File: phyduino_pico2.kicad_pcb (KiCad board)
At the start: 4 copper layers, 68.6 x 53.3 mm, 139 parts, among them J1 1.0-3PWT, J2 PM2.54-1*8, J3 PM2.54-1*10, J4 PM2.54-1*6, J5 PM2.54-1*8, J6 GT-USB-7047A, J7 HC-FPC-0.5-22P-CSH20, SW1 1977067-1, SW2 MINI MSK12CO2, U1 RP2350B, U10 AP63200WU, U108 TPS2121RUXR, U11 ESP32-C6-MINI-1-H4, U110 TPS2121RUXR, U2 GD25LE128EXHIGR, U3 IS66WVR8M8FBLL-104NLI, U4 XC6190AN157R-G, U5 ADS7038QRTERQ1, U7 ZD24C64A-MAGMT, U8 AP63200WU, U9 TPUSBLC6-2P6, Y1 XC32M4-12.000-F10NNFT

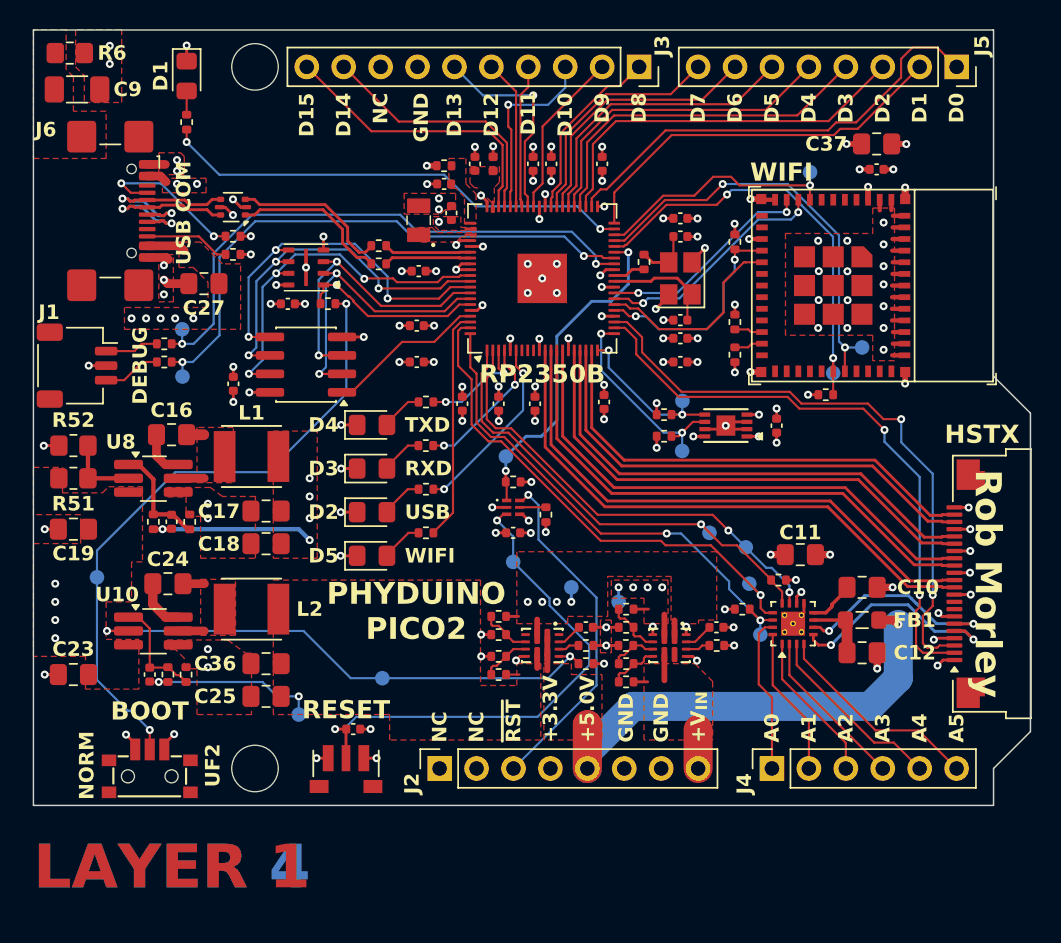
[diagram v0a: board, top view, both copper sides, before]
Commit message: Development update : Changed the power input and tree, removed led for communication status.
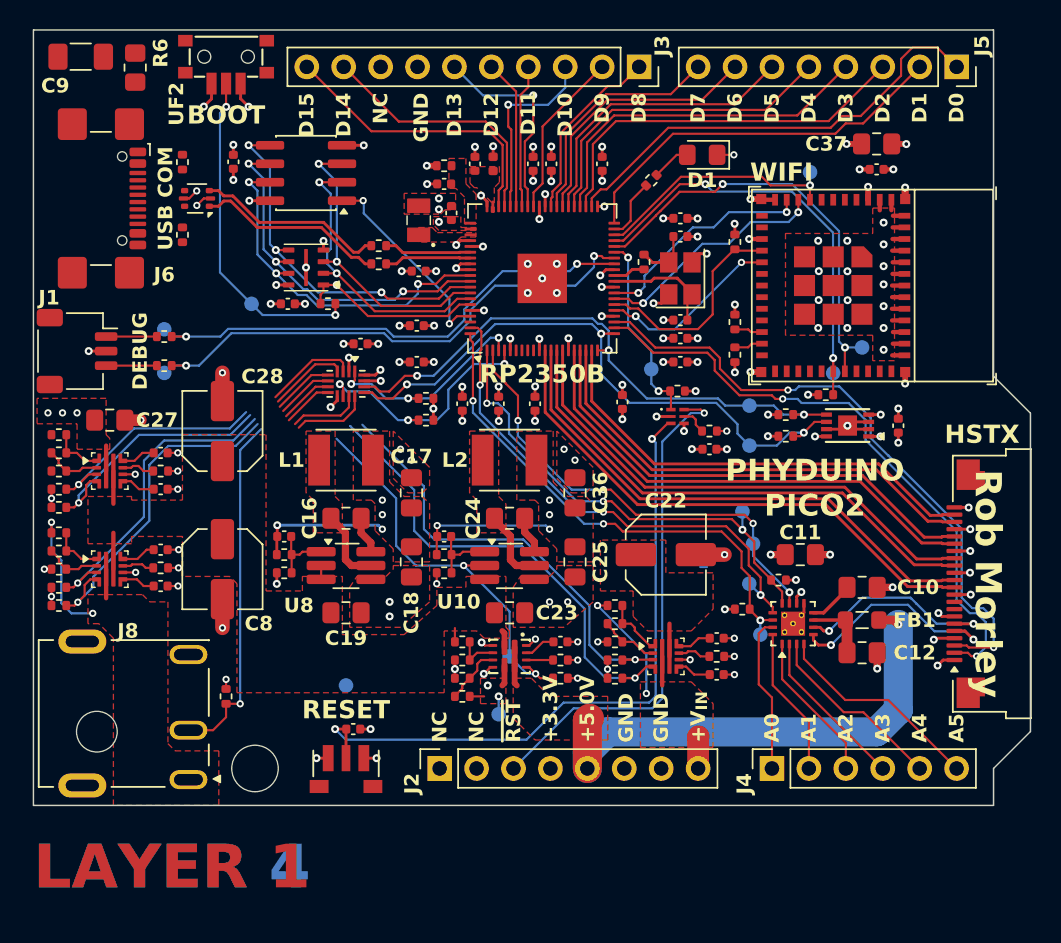
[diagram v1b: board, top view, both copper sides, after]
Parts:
- removed C134: 0.1µF, Capacitor_SMD:C_0402_1005Metric
- removed D2, D5: RED, LED_SMD:LED_0805_2012Metric_Pad1.15x1.40mm_HandSolder
- removed D3: ORANGE, LED_SMD:LED_0805_2012Metric_Pad1.15x1.40mm_HandSolder
- removed D4: GREEN, LED_SMD:LED_0805_2012Metric_Pad1.15x1.40mm_HandSolder
- removed H1: MountingHole, MountingHole [KL]:MountingHole_3.2mm_M3
- removed R140: 113kΩ, Resistor_SMD:R_0402_1005Metric
- removed R141: 432kΩ, Resistor_SMD:R_0402_1005Metric
- removed R142: 52.3kΩ, Resistor_SMD:R_0402_1005Metric
- removed R144, R145: 24.3kΩ, Resistor_SMD:R_0402_1005Metric
- removed R152: 35.7kΩ, Resistor_SMD:R_0402_1005Metric
- removed R51: 47kΩ, Resistor_SMD:R_0805_2012Metric_Pad1.20x1.40mm_HandSolder
- removed R52: 16.5kΩ, Resistor_SMD:R_0805_2012Metric_Pad1.20x1.40mm_HandSolder
- removed R53, R54, R60: 1.1kΩ, Resistor_SMD:R_0402_1005Metric
- removed TP16, TP17: TestPoint_Small, Component - Test point SMT [UL]:TestPoint_SameSky_CPG-47-TH-B
- removed U110: TPS2121RUXR, Package - QFN [UL]:VQFN-HR-12
- added C132: 0.033µF, Capacitor_SMD:C_0402_1005Metric, F.Cu at (38.5, 66.1)
- added C136: 1nF, Capacitor_SMD:C_0402_1005Metric, F.Cu at (38.5, 68.6)
- added C137: 0.033µF, Capacitor_SMD:C_0402_1005Metric, F.Cu at (76.7, 72.2)
- added C138: 1nF, Capacitor_SMD:C_0402_1005Metric, F.Cu at (76.7, 74.7)
- added C139: 0.1µF, Capacitor_SMD:C_0402_1005Metric, F.Cu at (38.5, 59.4)
- added C140: 1nF, Capacitor_SMD:C_0402_1005Metric, F.Cu at (38.5, 61.9)
- added C22: 100µF, Capacitor_SMD:C_Elec_5x5.4, F.Cu at (73.2, 66.4)
- added C28: 100µF, Capacitor_SMD:C_Elec_5x5.4, F.Cu at (42.7, 57.9)
- added C29: 0.1µF, Capacitor_SMD:C_0402_1005Metric, F.Cu at (52.2, 51.9)
- added C8: 100µF, Capacitor_SMD:C_Elec_5x5.4, F.Cu at (42.7, 67.4)
- added J8: 54-00127, Conector - Power [UL]:TENSILITY_54-00127, F.Cu at (33.1, 77.3)
- added R139: 1.1kΩ, Resistor_SMD:R_0402_1005Metric, F.Cu at (38.5, 67.3)
- added R143: 732kΩ, Resistor_SMD:R_0402_1005Metric, F.Cu at (31.5, 64.9)
- added R146: 215kΩ, Resistor_SMD:R_0402_1005Metric, F.Cu at (31.5, 66.2)
- added R147: 732kΩ, Resistor_SMD:R_0402_1005Metric, F.Cu at (69.7, 69.9)
- added R148: 215kΩ, Resistor_SMD:R_0402_1005Metric, F.Cu at (69.7, 71.2)
- added R149: 732kΩ, Resistor_SMD:R_0402_1005Metric, F.Cu at (31.5, 58.2)
- added R150: 53.6kΩ, Resistor_SMD:R_0402_1005Metric, F.Cu at (31.5, 67.4)
- added R151: 1.1kΩ, Resistor_SMD:R_0402_1005Metric, F.Cu at (76.7, 73.4)
- added R154: 53.6kΩ, Resistor_SMD:R_0402_1005Metric, F.Cu at (31.5, 59.4)
- added R155: 215kΩ, Resistor_SMD:R_0402_1005Metric, F.Cu at (31.5, 60.7)
- added R156: 1.1kΩ, Resistor_SMD:R_0402_1005Metric, F.Cu at (38.5, 60.7)
- added R157: 10kΩ, Resistor_SMD:R_0402_1005Metric, F.Cu at (31.5, 69.9)
- added R158: 10kΩ, Resistor_SMD:R_0402_1005Metric, F.Cu at (31.5, 68.7)
- added R159: 10kΩ, Resistor_SMD:R_0402_1005Metric, F.Cu at (69.7, 74.9)
- added R160: 10kΩ, Resistor_SMD:R_0402_1005Metric, F.Cu at (69.7, 73.7)
- added R161: 53.6kΩ, Resistor_SMD:R_0402_1005Metric, F.Cu at (69.7, 72.4)
- added R162: 10kΩ, Resistor_SMD:R_0402_1005Metric, F.Cu at (31.5, 63.2)
- added R163: 10kΩ, Resistor_SMD:R_0402_1005Metric, F.Cu at (31.5, 61.9)
- added R164: 10kΩ, Resistor_SMD:R_0402_1005Metric, F.Cu at (43.0, 76.2)
- added R64: 10kΩ, Resistor_SMD:R_0402_1005Metric, F.Cu at (56.7, 57.2)
- added U12: TPS259470ARPWR, Package - QFN [UL]:Texas_Instruments_VQFN-HR-10, F.Cu at (73.2, 73.4)
- added U13: TPS259470ARPWR, Package - QFN [UL]:Texas_Instruments_VQFN-HR-10, F.Cu at (35.0, 60.7)
- added U14: FXL6408UMX, Package - QFN [UL]:QFN40P260X180X55-16N, F.Cu at (51.2, 54.7)
- added U6: TPS259470ARPWR, Package - QFN [UL]:Texas_Instruments_VQFN-HR-10, F.Cu at (35.0, 67.4)
- R63: value 1.1kΩ -> 10kΩ
- U10, U8: footprint Package_TO_SOT_SMD [KL]:TSOT-23-6_HandSoldering -> Package_TO_SOT_SMD:TSOT-23-6_HandSoldering
- U9: footprint Package_TO_SOT_SMD [KL]:SOT-666 -> Package_TO_SOT_SMD:SOT-666
- moved SW2 49.8 mm to (43.0, 32.2), turned to 180 degrees
- moved D1 35.9 mm to (75.7, 38.9), turned to 180 degrees
- moved R46 32.2 mm to (72.2, 40.7), turned to 45 degrees
- moved C23 30.3 mm to (62.5, 70.4), turned to 0 degrees
- moved U10 24.9 mm to (62.5, 67.2)
- moved C36 24.3 mm to (67.0, 62.2), turned to 90 degrees
- moved C24 23.9 mm to (62.5, 63.9), turned to 180 degrees
- moved C25 23.2 mm to (67.0, 66.9), turned to -90 degrees
- moved C7 22.4 mm to (58.0, 65.2), turned to 0 degrees
- moved TP25 21.6 mm to (44.7, 49.2)
- moved R58 20.7 mm to (58.0, 66.4), turned to 0 degrees
- moved L2 20.5 mm to (62.5, 59.9)
- moved C19 19.6 mm to (51.2, 70.4), turned to 0 degrees
- moved R59 19.1 mm to (58.0, 67.7), turned to 180 degrees
- moved C6 15.3 mm to (43.5, 39.4)
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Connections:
- net +VUSB_COMM renamed +VUSB
- net /Communication & Power Delivery/DCDC_3V3_BST renamed /Power/DCDC_3V3_BST
- net /Communication & Power Delivery/DCDC_3V3_FB renamed /Power/DCDC_3V3_FB
- net /Communication & Power Delivery/DCDC_3V3_SW renamed /Power/DCDC_3V3_SW
- net /Communication & Power Delivery/DCDC_5V0_BST renamed /Power/DCDC_5V0_BST
- net /Communication & Power Delivery/DCDC_5V0_EN renamed /Power/DCDC_5V0_EN
- net /Communication & Power Delivery/DCDC_5V0_FB renamed /Power/DCDC_5V0_FB
- net /Communication & Power Delivery/DCDC_5V0_SW renamed /Power/DCDC_5V0_SW
- net /Communication & Power Delivery/PMUX_LIM renamed /Power/PMUX_LIM
- net /Communication & Power Delivery/PMUX_OV1 renamed /Power/PMUX_OV1
- net /Communication & Power Delivery/PMUX_OV2 renamed /Power/PMUX_OV2
- net /Communication & Power Delivery/PMUX_SS renamed /Power/PMUX_SS
- net /Communication & Power Delivery/USB_CC1 renamed /USB_CC1
- net /Communication & Power Delivery/USB_CC2 renamed /USB_CC2
- net /Communication & Power Delivery/USB_COM_D_N renamed /USB_COM_D_N
- net /Communication & Power Delivery/USB_COM_D_P renamed /USB_COM_D_P
- net /Communication & Power Delivery/USB_D_N renamed /Microcontroller/USB_D_N
- net /Communication & Power Delivery/USB_D_P renamed /Microcontroller/USB_D_P
- net /Communication & Power Delivery/WIFI_BOOT0 renamed /Wireless Communication/WIFI_BOOT0
- net /Communication & Power Delivery/WIFI_BOOT1 renamed /Wireless Communication/WIFI_BOOT1
- net /Communication & Power Delivery/WIFI_ENA renamed /Microcontroller/WIFI_ENA
- net /Communication & Power Delivery/XTAL_32K_N renamed /Wireless Communication/XTAL_32K_N
- net /Communication & Power Delivery/XTAL_32K_P renamed /Wireless Communication/XTAL_32K_P
- C19 pad 1: +VMUX -> +VIN_REG
- C23 pad 1: +VMUX -> +VIN_REG
- C9 pad 1: /Communication & Power Delivery/USB_COM_SHIELD -> /USB_COM_SHIELD
- R138 pad 2: +VMUX -> +VIN_REG
- R50 pad 2: /Communication & Power Delivery/WIFI_DL_UART_RX -> /Microcontroller/WIFI_DL_UART_RX
- R55 pad 2: /Communication & Power Delivery/WIFI_AT_UART_RX -> /Microcontroller/WIFI_UART_RX
- R6 pad 1: /Communication & Power Delivery/USB_COM_SHIELD -> /USB_COM_SHIELD
- R63 pad 1: /Microcontroller/CONNECTED_WIFI -> +3.3V
- R63 pad 2: /Microcontroller/WIFI_CONNECTED -> /Microcontroller/IO_EXP_~{INT}
- TP8 pad 1: /Communication & Power Delivery/WIFI_DL_UART_TX -> /Microcontroller/WIFI_DL_UART_TX
- TP9 pad 1: /Communication & Power Delivery/WIFI_DL_UART_RX -> /Microcontroller/WIFI_DL_UART_RX
- U1 pad 25: /Communication & Power Delivery/WIFI_AT_UART_RX -> /Microcontroller/WIFI_UART_TX
- U1 pad 26: /Communication & Power Delivery/WIFI_AT_UART_TX -> /Microcontroller/WIFI_UART_RX
- U1 pad 27: /Communication & Power Delivery/WIFI_AT_UART_RTS -> /Microcontroller/WIFI_UART_CTS
- U1 pad 28: /Communication & Power Delivery/WIFI_AT_UART_CTS -> /Microcontroller/WIFI_UART_RTS
- U1 pad 3: /Microcontroller/TXD_COMM -> /Microcontroller/IO_EXP_~{INT}
- U1 pad 36: /Communication & Power Delivery/WIFI_DL_UART_RX -> /Microcontroller/WIFI_DL_UART_TX
- U1 pad 37: /Communication & Power Delivery/WIFI_DL_UART_TX -> /Microcontroller/WIFI_DL_UART_RX
- U1 pad 4: /Microcontroller/RXD_COMM -> /Microcontroller/IO_EXP_~{RST}
- U1 pad 6: /Microcontroller/CONNECTED_COMM -> unconnected-(U1-GPIO8-Pad6)
- U1 pad 78: /Microcontroller/CONNECTED_WIFI -> unconnected-(U1-GPIO1-Pad78)
- U10 pad 3: +VMUX -> +VIN_REG
- U108 pad 2: +VMUX -> +VIN_REG
- U11 pad 10: /Communication & Power Delivery/WIFI_AT_UART_CTS -> /Microcontroller/WIFI_UART_CTS
- U11 pad 15: /Communication & Power Delivery/WIFI_AT_UART_RX -> /Microcontroller/WIFI_UART_RX
- U11 pad 16: /Communication & Power Delivery/WIFI_AT_UART_TX -> /Microcontroller/WIFI_UART_TX
- U11 pad 30: /Communication & Power Delivery/WIFI_DL_UART_RX -> /Microcontroller/WIFI_DL_UART_RX
- U11 pad 31: /Communication & Power Delivery/WIFI_DL_UART_TX -> /Microcontroller/WIFI_DL_UART_TX
- U11 pad 9: /Communication & Power Delivery/WIFI_AT_UART_RTS -> /Microcontroller/WIFI_UART_RTS
- U8 pad 2: /Communication & Power Delivery/DCDC_3V3_EN -> +VIN_REG
- U8 pad 3: +VMUX -> +VIN_REG
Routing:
- net /Microcontroller/SHIELD_~{FLT}: track 0.00 -> 36.5 mm, vias 0 -> 1
- net /Microcontroller/SHIELD_AUXOFF: track 0.00 -> 34.8 mm, vias 0 -> 1
- net (no net): track 0.00 -> 31.7 mm, vias 0 -> 4
- net /Microcontroller/WIFI_DL_UART_RX: track 0.00 -> 30.2 mm, vias 0 -> 2
- net /Communication & Power Delivery/WIFI_DL_UART_RX: track 29.9 -> 0.00 mm, vias 2 -> 0
- net /Microcontroller/~{EXT_PWR}: track 0.00 -> 29.6 mm, vias 0 -> 1
- net /Microcontroller/WIFI_DL_UART_TX: track 0.00 -> 29.6 mm, vias 0 -> 2
- net /Communication & Power Delivery/WIFI_DL_UART_TX: track 29.2 -> 0.00 mm, vias 2 -> 0
- net /Microcontroller/BUILTIN_LED: track 32.7 -> 4.23 mm, vias 2 -> 0
- net /Microcontroller/EXT_~{FLT}: track 0.00 -> 28.3 mm, vias 0 -> 1
- net /Microcontroller/I2C0_SDA: track 11.6 -> 39.5 mm, vias 2 -> 3
- net /Microcontroller/I2C0_SCL: track 14.7 -> 42.0 mm, vias 2 -> 3
- net /Microcontroller/EXT_AUXOFF: track 0.00 -> 25.1 mm, vias 0 -> 1
- net /Microcontroller/USB_~{FLT}: track 0.00 -> 22.1 mm, vias 0 -> 1
- net /Microcontroller/USB_AUXOFF: track 0.00 -> 21.6 mm, vias 0 -> 1
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- added copper zone on In2.Cu, net (none)
- added copper zone on F.Cu, net +VIN_REG
- added copper zone on F.Cu, net /Power/+EXTERNAL_POWER
- removed copper zone on F.Cu, net +VMUX
- removed copper zone on In2.Cu, net +VMUX
- removed copper zone on In2.Cu, net +VUSB
- removed copper zone on F.Cu, net /Communication & Power Delivery/USB_COM_SHIELD
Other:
- board text added: "PHYDUINO PICO2 REVA0 OCT 2026"
- board text removed: "NORM"
- board text removed: "PHYDUINO PICO2 REVA JULY 2026"
- board text removed: "RXD"
- board text removed: "TXD"
- board text removed: "USB"

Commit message: Development update : Initial design review changes and PCB routing.
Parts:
- removed R18: 10kΩ, Resistor_SMD:R_0402_1005Metric
- removed SW2: MINI MSK12CO2, Mechanical - Switch [UL]:Switch_Slide_ShouHan_MINI_MSK12CO2
- removed TP25: TestPoint_Small, Component - Test point SMT [UL]:TestPoint_SameSky_CPG-47-TH-B
- removed U4: XC6190AN157R-G, Package - DFN [UL]:PHODET_VBPW34S
- added C58: 4700pF, Capacitor_SMD:C_0402_1005Metric, F.Cu at (81.7, 59.4)
- added C59: 1000pF, Capacitor_SMD:C_0402_1005Metric, F.Cu at (79.5, 59.4)
- added G***: LOGO, Drawings library [UL]:qwiic_6mm, F.Cu at (42.5, 38.2)
- added J9: SM04B-SRSS-TB, Connector_JST:JST_SH_SM04B-SRSS-TB_1x04-1MP_P1.00mm_Horizontal, F.Cu at (42.5, 33.7)
- added R21: 10kΩ, Resistor_SMD:R_0402_1005Metric, F.Cu at (84.2, 56.7)
- added R22: 10kΩ, Resistor_SMD:R_0402_1005Metric, F.Cu at (81.5, 55.4)
- added R51: 10kΩ, Resistor_SMD:R_0402_1005Metric, F.Cu at (74.5, 37.9)
- added R52: 10kΩ, Resistor_SMD:R_0402_1005Metric, F.Cu at (76.7, 52.7)
- added U15: TPS3424C11EF2ADRLR, Pacakge - SOT [UL]:SOT-5x3_DRL0008A_TEX, F.Cu at (80.5, 57.4)
- C132, C137: value 0.033µF -> 0.1µF
- FB1: value MLB1005F-221T -> ~
- J2, J5: value PM2.54-1*8 -> PPPC081LFBN-RC
- J3: value PM2.54-1*10 -> PPPC101LFBN-RC
- J4: value PM2.54-1*6 -> PPPC061LFBN-RC
- R135, R138: value 21kΩ -> 42.2kΩ
- R136, R137, R49: value 5.1kΩ -> 10kΩ
- R42, R43, R61, R62: value 4.7kΩ -> 5.1kΩ
- R44, R45: value 1.1kΩ -> 10kΩ
- U2: value GD25LE128EXHIGR -> AT25QF128A-SHB-T; footprint Package - SON [UL]:USON-8-2EP_3x3mm_P0.8mm_EP0.8x.02mm -> Package_SO:SOIC-8_5.3x5.3mm_P1.27mm
- moved C21 46.6 mm to (44.0, 46.4), turned to 180 degrees
- moved U7 43.4 mm to (43.2, 48.7), turned to 0 degrees
- moved TP3 36.8 mm to (44.0, 47.4)
- moved R62 35.8 mm to (47.0, 48.7), turned to 180 degrees
- moved TP1 35.5 mm to (44.0, 50.4)
- moved R61 35.2 mm to (47.0, 49.9), turned to 180 degrees
- moved C6 33.7 mm to (76.7, 44.9), turned to -90 degrees
- moved C1 30.3 mm to (76.7, 56.2), turned to -90 degrees
- moved D1 29.1 mm to (58.2, 62.2), turned to 90 degrees
- moved R49 26.8 mm to (76.7, 50.4), turned to -90 degrees
- moved C129 26.4 mm to (50.5, 41.7), turned to 180 degrees
- moved U2 25.3 mm to (73.1, 52.3), turned to -90 degrees
- moved C135 25.2 mm to (50.5, 51.7), turned to 180 degrees
- moved C125 25.1 mm to (50.5, 43.3), turned to 180 degrees
- moved U3 24.7 mm to (73.1, 42.4), turned to -90 degrees
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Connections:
- net +VIN renamed +V_{IN}
- net +VUSB renamed +V_{USB}
- net /Power/+EXTERNAL_POWER renamed +V_{EXTERNAL}
- C57 pad 1: /Microcontroller/SW_~{RESET} -> /Microcontroller/EXT_~{RESET}
- J2 pad 2: unconnected-(J2-Pin_2-Pad2) -> +3.3V
- R44 pad 1: /Wireless Communication/WIFI_BOOT1 -> +3.3V
- R44 pad 2: GND -> /Microcontroller/WIFI_BOOT1
- R49 pad 1: /Microcontroller/BOOTMODE -> /Microcontroller/FLASH_~{CS}
- R49 pad 2: /Microcontroller/FLASH_~{CS} -> /Microcontroller/MCU_BOOT_SEL
- R50 pad 2: /Microcontroller/WIFI_DL_UART_RX -> /Microcontroller/WIFI_DL_UART_TX
- R55 pad 2: /Microcontroller/WIFI_UART_RX -> /Microcontroller/WIFI_UART_TX
- R61 pad 2: /Microcontroller/I2C0_SDA -> /Microcontroller/I2C1_SDA
- R62 pad 2: /Microcontroller/I2C0_SCL -> /Microcontroller/I2C1_SCL
- SW1 pad 2: /Microcontroller/SW_~{RESET} -> /Microcontroller/EXT_~{RESET}
- TP1 pad 1: /Microcontroller/I2C0_SDA -> /Microcontroller/I2C1_SDA
- TP20 pad 1: /Microcontroller/ADC_MISO -> /Microcontroller/ADC_SCK
- TP24 pad 1: /Microcontroller/ADC_SCK -> /Microcontroller/ADC_MISO
- TP26 pad 1: /Microcontroller/SW_~{RESET} -> /Microcontroller/EXT_~{RESET}
- TP3 pad 1: /Microcontroller/I2C0_SCL -> /Microcontroller/I2C1_SCL
- TP8 pad 1: /Microcontroller/WIFI_DL_UART_TX -> /Microcontroller/WIFI_DL_UART_RX
- TP9 pad 1: /Microcontroller/WIFI_DL_UART_RX -> /Microcontroller/WIFI_DL_UART_TX
- U1 pad 1: /Microcontroller/ADC_MISO -> /Microcontroller/D2
- U1 pad 2: /Microcontroller/ADC_nCS -> /Microcontroller/D3
- U1 pad 20: /Microcontroller/I2C0_SDA -> /Microcontroller/D12
- U1 pad 21: /Microcontroller/I2C0_SCL -> /Microcontroller/D10
- U1 pad 22: /Microcontroller/HS_I2C1_SDA -> /Microcontroller/D13
- U1 pad 23: /Microcontroller/HS_I2C1_SCL -> /Microcontroller/D11
- U1 pad 25: /Microcontroller/WIFI_UART_TX -> /Microcontroller/D14
- U1 pad 26: /Microcontroller/WIFI_UART_RX -> /Microcontroller/D15
- U1 pad 27: /Microcontroller/WIFI_UART_CTS -> /Microcontroller/WIFI_DL_UART_TX
- U1 pad 28: /Microcontroller/WIFI_UART_RTS -> /Microcontroller/WIFI_DL_UART_RX
- U1 pad 3: /Microcontroller/IO_EXP_~{INT} -> /Microcontroller/D4
- U1 pad 36: /Microcontroller/WIFI_DL_UART_TX -> /Microcontroller/WIFI_UART_TX
- U1 pad 37: /Microcontroller/WIFI_DL_UART_RX -> /Microcontroller/WIFI_UART_RX
- U1 pad 38: /Microcontroller/WIFI_ENA -> /Microcontroller/WIFI_UART_CTS
- U1 pad 39: /Microcontroller/BUILTIN_LED -> /Microcontroller/WIFI_UART_RTS
- U1 pad 4: /Microcontroller/IO_EXP_~{RST} -> /Microcontroller/D5
- U1 pad 40: /Microcontroller/D1 -> /Microcontroller/WIFI_BOOT1
- U1 pad 42: /Microcontroller/D0 -> unconnected-(U1-GPIO33-Pad42)
- U1 pad 43: /Microcontroller/D2 -> unconnected-(U1-GPIO34-Pad43)
- U1 pad 44: /Microcontroller/D3 -> unconnected-(U1-GPIO35-Pad44)
- U1 pad 45: /Microcontroller/D4 -> /Microcontroller/IO_EXP_~{RST}
- U1 pad 46: /Microcontroller/D5 -> unconnected-(U1-GPIO37-Pad46)
- U1 pad 47: /Microcontroller/D6 -> /Microcontroller/HS_I2C1_SDA
- U1 pad 48: /Microcontroller/D7 -> /Microcontroller/HS_I2C1_SCL
- U1 pad 49: /Microcontroller/D8 -> /Microcontroller/BUILTIN_LED
- U1 pad 52: /Microcontroller/D9 -> /Microcontroller/IO_EXP_~{INT}
- U1 pad 53: /Microcontroller/D13 -> /Microcontroller/I2C1_SDA
- U1 pad 54: /Microcontroller/D11 -> /Microcontroller/I2C1_SCL
- U1 pad 55: /Microcontroller/D12 -> /Microcontroller/ADC_MISO
- U1 pad 56: /Microcontroller/D10 -> /Microcontroller/ADC_nCS
- U1 pad 57: /Microcontroller/D14 -> /Microcontroller/ADC_SCK
- U1 pad 58: /Microcontroller/D15 -> /Microcontroller/ADC_MOSI
- U1 pad 6: unconnected-(U1-GPIO8-Pad6) -> /Microcontroller/D6
- U1 pad 7: unconnected-(U1-GPIO9-Pad7) -> /Microcontroller/D7
- U1 pad 78: unconnected-(U1-GPIO1-Pad78) -> /Microcontroller/WIFI_ENA
- U1 pad 79: /Microcontroller/ADC_SCK -> /Microcontroller/D1
- U1 pad 8: unconnected-(U1-GPIO10-Pad8) -> /Microcontroller/D8
- U1 pad 80: /Microcontroller/ADC_MOSI -> /Microcontroller/D0
- U1 pad 9: unconnected-(U1-GPIO11-Pad9) -> /Microcontroller/D9
- U11 pad 10: /Microcontroller/WIFI_UART_CTS -> /Microcontroller/WIFI_UART_RTS
- U11 pad 15: /Microcontroller/WIFI_UART_RX -> /Microcontroller/WIFI_UART_TX
- U11 pad 16: /Microcontroller/WIFI_UART_TX -> /Microcontroller/WIFI_UART_RX
- U11 pad 23: /Wireless Communication/WIFI_BOOT1 -> /Microcontroller/WIFI_BOOT1
- U11 pad 30: /Microcontroller/WIFI_DL_UART_RX -> /Microcontroller/WIFI_DL_UART_TX
- U11 pad 31: /Microcontroller/WIFI_DL_UART_TX -> /Microcontroller/WIFI_DL_UART_RX
- U11 pad 9: /Microcontroller/WIFI_UART_RTS -> /Microcontroller/WIFI_UART_CTS
- U14 pad 11: /Microcontroller/EXT_~{FLT} -> /Microcontroller/SHIELD_~{FLT}
- U14 pad 12: /Microcontroller/~{EXT_PWR} -> /Microcontroller/SHIELD_AUXOFF
- U14 pad 13: /Microcontroller/I2C0_SCL -> /Microcontroller/I2C1_SCL
- U14 pad 14: /Microcontroller/I2C0_SDA -> /Microcontroller/I2C1_SDA
- U14 pad 3: /Power/DCDC_5V0_EN -> /Microcontroller/USB_AUXOFF
- U14 pad 4: /Microcontroller/USB_AUXOFF -> /Microcontroller/USB_~{FLT}
- U14 pad 5: /Microcontroller/USB_~{FLT} -> /Microcontroller/EXT_AUXOFF
- U14 pad 6: /Microcontroller/SHIELD_AUXOFF -> /Microcontroller/EXT_~{FLT}
- U14 pad 7: /Microcontroller/SHIELD_~{FLT} -> /Microcontroller/~{EXT_PWR}
- U14 pad 8: /Microcontroller/EXT_AUXOFF -> /Power/DCDC_5V0_EN
- U7 pad 5: /Microcontroller/I2C0_SDA -> /Microcontroller/I2C1_SDA
- U7 pad 6: /Microcontroller/I2C0_SCL -> /Microcontroller/I2C1_SCL
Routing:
- net /Microcontroller/WIFI_UART_CTS: track 0.00 -> 59.9 mm, vias 0 -> 2
- net /Microcontroller/WIFI_UART_RTS: track 0.00 -> 58.6 mm, vias 0 -> 2
- net /Microcontroller/WIFI_UART_TX: track 12.6 -> 66.3 mm
- net /Microcontroller/WIFI_UART_RX: track 14.9 -> 61.2 mm, vias 0 -> 3
- net /Microcontroller/SW_~{RESET}: track 45.9 -> 0.00 mm, vias 2 -> 0
- net /Microcontroller/WIFI_BOOT1: track 0.00 -> 43.4 mm, vias 0 -> 2
- net /Microcontroller/I2C0_SCL: track 42.0 -> 0.00 mm, vias 3 -> 0
- net /Microcontroller/I2C0_SDA: track 39.5 -> 0.00 mm, vias 3 -> 0
- net /Microcontroller/I2C1_SCL: track 0.00 -> 32.5 mm, vias 0 -> 3
- net (no net): track 31.7 -> 0.00 mm, vias 4 -> 0
- net /Microcontroller/I2C1_SDA: track 0.00 -> 31.0 mm, vias 0 -> 3
- net /Microcontroller/WIFI_DL_UART_RX: track 30.2 -> 59.5 mm
- net /Microcontroller/WIFI_DL_UART_TX: track 29.6 -> 58.3 mm
- net /Microcontroller/USB_IO_D_N: track 6.00 -> 33.1 mm, vias 0 -> 2
- net /Microcontroller/USB_IO_D_P: track 5.98 -> 31.9 mm, vias 0 -> 2
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- added copper zone on In2.Cu, net +5.0V_DCDC
- added copper zone on In2.Cu, net +VIN_REG
- added copper zone on In2.Cu, net +V_{USB}
- added copper zone on F.Cu, net /USB_COM_SHIELD
- removed copper zone on In2.Cu, net (none)
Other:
- board text removed: "BOOT"
- board text removed: "UF2"
- board text removed: "USB COM"
